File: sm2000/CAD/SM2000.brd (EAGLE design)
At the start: 160 x 160 mm, 405 parts, among them CN1 HDR100-3, CN2 ST-3509, CN3 HDR100-3, CN4 JS-MU3-002, CN5 DS-0518, CN6 ST-3509, CN7 ST-3509, J1 JMP-2PIN, J10 JMPR-2X2, J11 JMPR-2X2, J12 JMPR-2X2, J13 JMPR-2X2, J14 JMPR-2X2, J2 HDR100-7, J3 JMP-2PIN, J4 CONN-BOOM-XH-2A, J5 JMP-2PIN, J6 JMPR-2X2, J7 JMPR-2X2, J8 JMPR-2X2, J9 JMPR-2X2, P6 TPAD50, P7 TPAD50, P8 TPAD50, P9 TPAD50, Q1 MMBT3904, Q10 MMBT3904, Q11 BFR92, Q12 BFQ19, Q13 RD01MUS2, Q14 MMBT3904, Q15 MMBT3904, Q16 MMBT3904, Q17 MMBT3906, Q2 STR2P3LLH6, Q3 MMBT3904, Q4 STR2P3LLH6, Q5 MMBT3904, Q6 MMBT3904, Q7 MMBT3904, Q8 MMBT3904, Q9 MMBT3904, SW1 TS-02B, SW2 SW-LC2259, SW3 TS-026, SW4 TS-026, SW5 SW-LC2259EENP, U1 STM32F405VGT6, U10 LM386M-1, U11 ADE-1, U12 PGA-103+, U13 LMV341, U14 SI5351A, U15 SI570, U16 SA612A, U2 STMPS2141, U3 EMIF02-USB03F2, U4 DNL, U5 L78M09, U6 LD1117AS-33, U7 LMV341, U8 LD1117AS-33, U9 TPS54329E, X1 BU-SMA-H

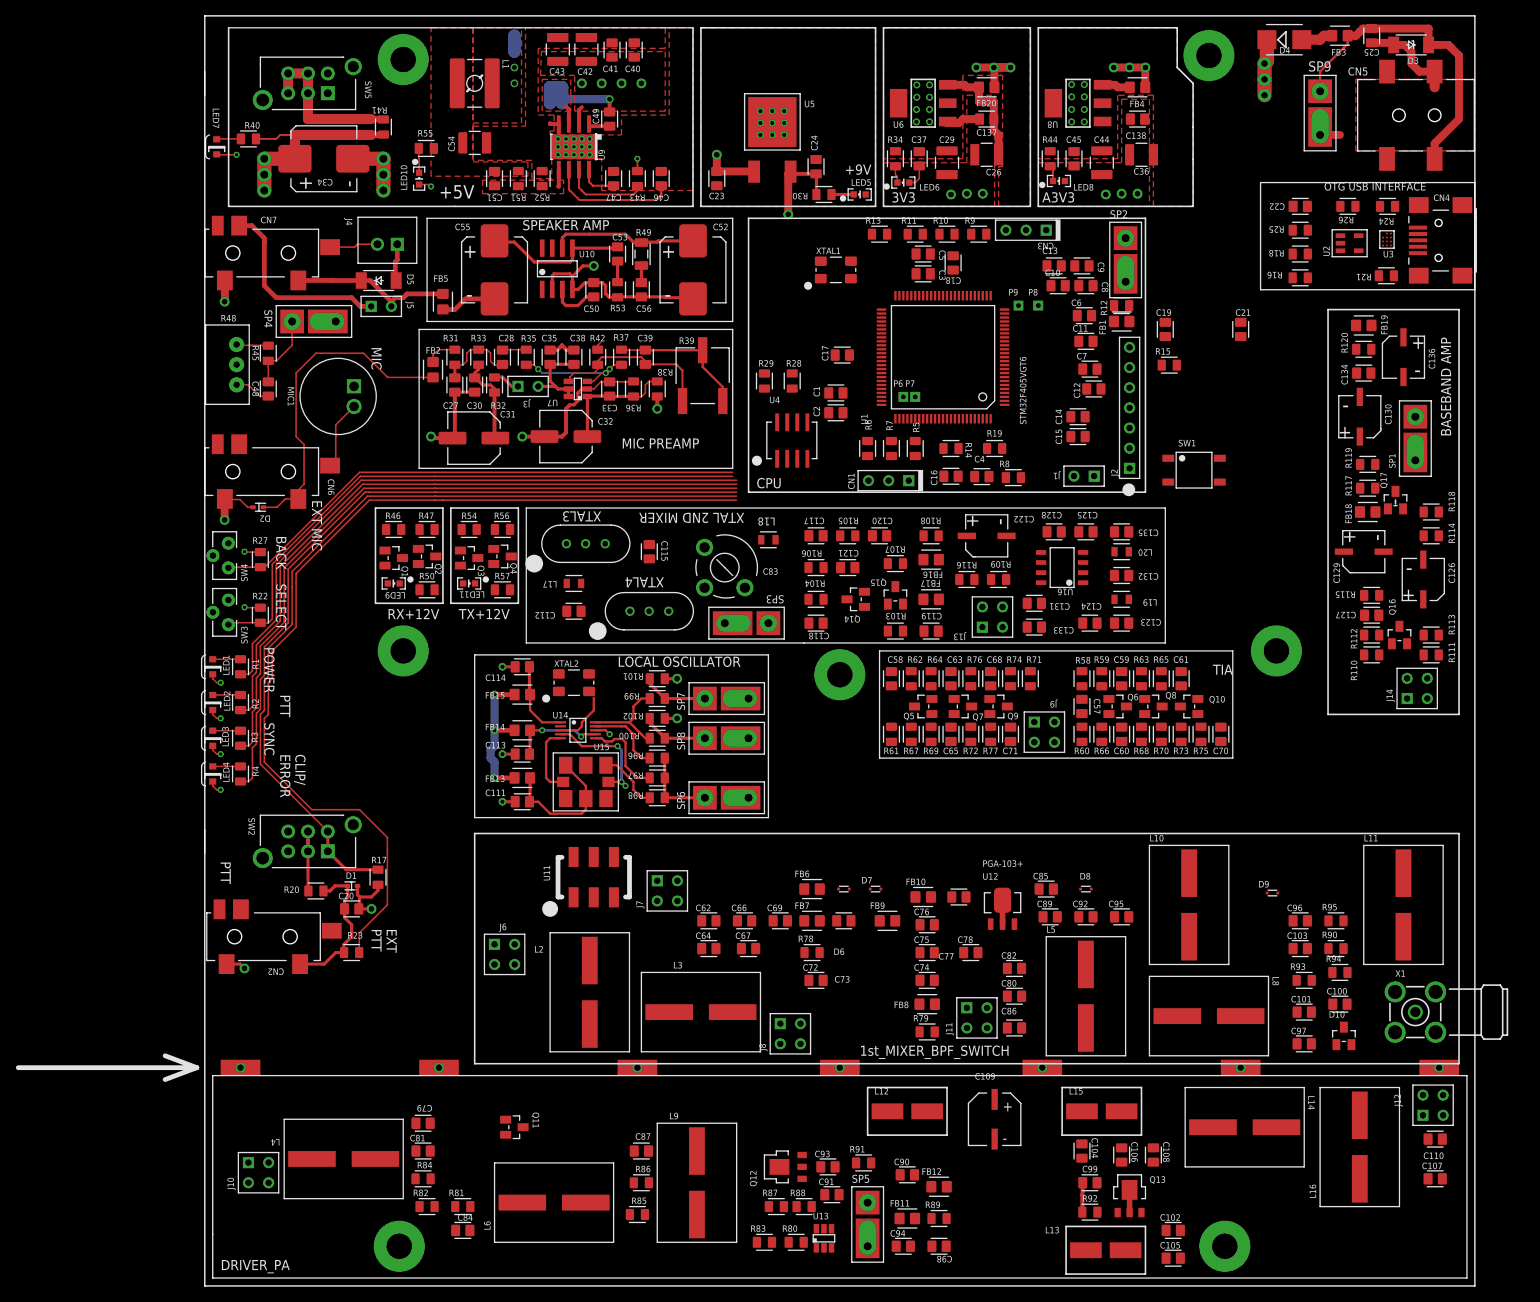
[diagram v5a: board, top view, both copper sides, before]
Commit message: Current status as of 4/4/16 RGB
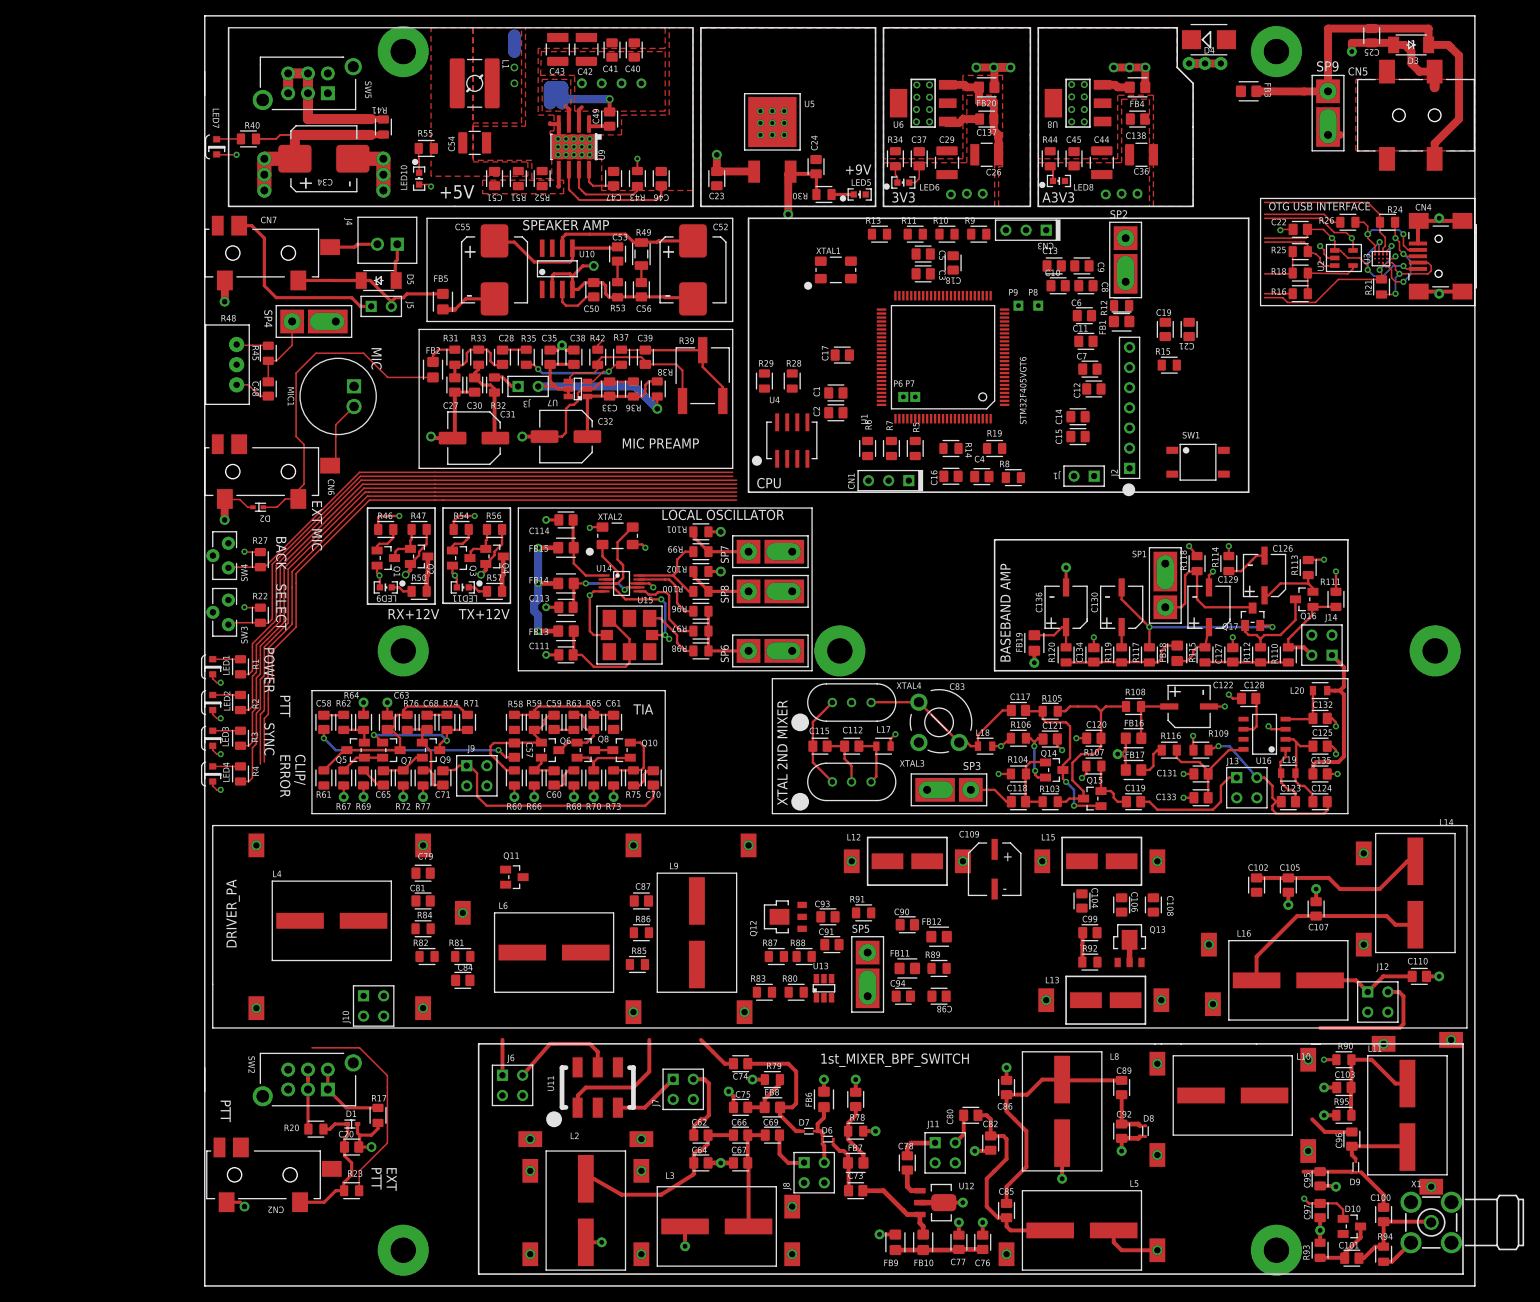
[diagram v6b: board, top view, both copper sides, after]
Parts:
- added PAD1, PAD2, PAD3, PAD4, PAD5, PAD6, PAD7: MTG-PAD-3.2, _RoweTel:MTG-PAD-3.2
- added S10, S11, S12, S13, S14, S15, S16, S17, S18, S19, S20, S21, S22, S23, S24, S25, S26, S27, S28, S29, S30, S31, S32, S33, S34, S35, S36, S8, S9: SGND, _RoweTel:SGND
- moved Q7 72.2 mm to (23.5, 67.5)
- moved C57 71.7 mm to (39.0, 67.5)
- moved C58 71.7 mm to (15.0, 71.0)
- moved C59 71.7 mm to (44.0, 71.0)
- moved C60 71.7 mm to (44.0, 64.0)
- moved C61 71.7 mm to (51.5, 71.0)
- moved C65 71.7 mm to (22.5, 64.0)
- moved C70 71.7 mm to (56.5, 64.0), turned to 90 degrees
- moved C71 71.7 mm to (30.0, 64.0)
- moved J9 71.7 mm to (33.0, 63.0)
- moved Q10 71.7 mm to (52.5, 67.5)
- moved Q5 71.7 mm to (19.0, 67.5)
- moved Q6 71.7 mm to (43.5, 67.5)
- moved Q8 71.7 mm to (48.0, 67.5)
- moved Q9 71.7 mm to (28.5, 67.5)
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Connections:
- net GND: now also PAD1.P$1, PAD2.P$1, PAD3.P$1, PAD4.P$1, PAD5.P$1, PAD6.P$1, PAD7.P$1, S1.1, S10.1, S11.1, S12.1, S13.1, S14.1, S15.1, S16.1, S17.1, S18.1, S19.1, S2.1, S20.1, S21.1, S22.1, S23.1, S24.1, S25.1, S26.1, S27.1, S28.1, S29.1, S3.1, S30.1, S31.1, S32.1, S33.1, S34.1, S35.1, S36.1, S4.1, S5.1, S6.1, S7.1, S8.1, S9.1; no longer S1.SGND, S2.SGND, S3.SGND, S4.SGND, S5.SGND, S6.SGND, S7.SGND
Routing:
- net GND: track 173.1 -> 323.4 mm, vias 50 -> 105
- net TIA_OUT: track 0.00 -> 32.6 mm
- net N$137: track 0.00 -> 31.1 mm
- net TIAIN: track 0.00 -> 30.6 mm, vias 0 -> 2
- net VBUS: track 0.00 -> 30.2 mm, vias 0 -> 4
- net N$92: track 0.00 -> 27.1 mm
- net N$140: track 0.00 -> 26.8 mm
- net N$106: track 0.00 -> 26.1 mm, vias 0 -> 2
- net N$9: track 0.00 -> 25.6 mm
- net N$136: track 0.00 -> 25.5 mm
- net N$21: track 0.00 -> 24.0 mm
- net N$49: track 0.00 -> 22.8 mm, vias 0 -> 1
- net OTG_DM: track 0.00 -> 22.7 mm, vias 0 -> 2
- net N$145: track 0.00 -> 22.7 mm
- net PA_OUTPUT: track 0.00 -> 22.1 mm
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
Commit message: LAYOUT UPDATES as of 4/13/16  RGB 80 NODES to COMPLETE
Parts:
- added S37, S38, S39, S40, S41, S42, S43: SGND, _RoweTel:SGND
- moved R83 87.5 mm to (71.5, 124.5)
- moved U13 85.0 mm to (75.5, 122.5)
- moved R80 84.1 mm to (71.5, 121.0)
- moved J1 41.3 mm to (70.5, 111.0), turned to 0 degrees
- moved C4 36.2 mm to (127.0, 123.6), turned to 90 degrees
- moved R8 35.5 mm to (129.8, 123.6), turned to 270 degrees
- moved XTAL1 35.3 mm to (112.5, 115.5), turned to 270 degrees
- moved C91 28.9 mm to (51.0, 50.0)
- moved R88 27.1 mm to (51.0, 53.0), turned to 180 degrees
- moved SW1 26.5 mm to (128.2, 130.1), turned to 90 degrees
- moved S18 26.2 mm to (77.5, 34.5)
- moved L14 24.5 mm to (128.0, 50.0)
- moved U4 23.0 mm to (72.5, 129.5)
- moved C64 22.3 mm to (41.0, 9.50), turned to 270 degrees
- moved J9 21.8 mm to (53.5, 70.5)
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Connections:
- net GND: now also S37.1, S38.1, S39.1, S40.1, S41.1, S42.1, S43.1
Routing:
- net +9V: track 11.6 -> 296.2 mm, vias 1 -> 5
- net +5V: track 35.6 -> 310.3 mm, vias 9 -> 12
- net TX+12V: track 7.56 -> 256.8 mm, vias 2 -> 11
- net 3V3: track 36.3 -> 216.5 mm, vias 13 -> 22
- net A3V3: track 30.7 -> 168.9 mm, vias 10 -> 15
- net GND: track 323.4 -> 454.2 mm, vias 105 -> 120
- net RX+12V: track 6.01 -> 135.7 mm, vias 1 -> 4
- net +VIN: track 164.7 -> 261.0 mm, vias 11 -> 10
- net RX-2ND-LO: track 10.1 -> 84.7 mm
- net AIN3: track 6.63 -> 78.0 mm, vias 1 -> 2
- net TX-2ND-LO: track 9.99 -> 69.8 mm, vias 1 -> 0
- net 1ST_LO: track 25.8 -> 82.0 mm, vias 0 -> 2
- net !EXT-PTT!: track 111.7 -> 167.4 mm
- net VGG: track 0.00 -> 52.3 mm, vias 0 -> 1
- net DRIVER/PA_INPUT: track 5.34 -> 57.4 mm
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- added copper zone on layer 15, net 3V3
- added copper zone on layer 16, net 3V3
- added copper zone on layer 15, net A3V3
- added copper zone on layer 16, net A3V3
- added copper zone on layer 15, net SW
- removed copper zone on layer 3, net 3V3
- removed copper zone on layer 3, net A3V3
- removed copper zone on layer 3, net SW

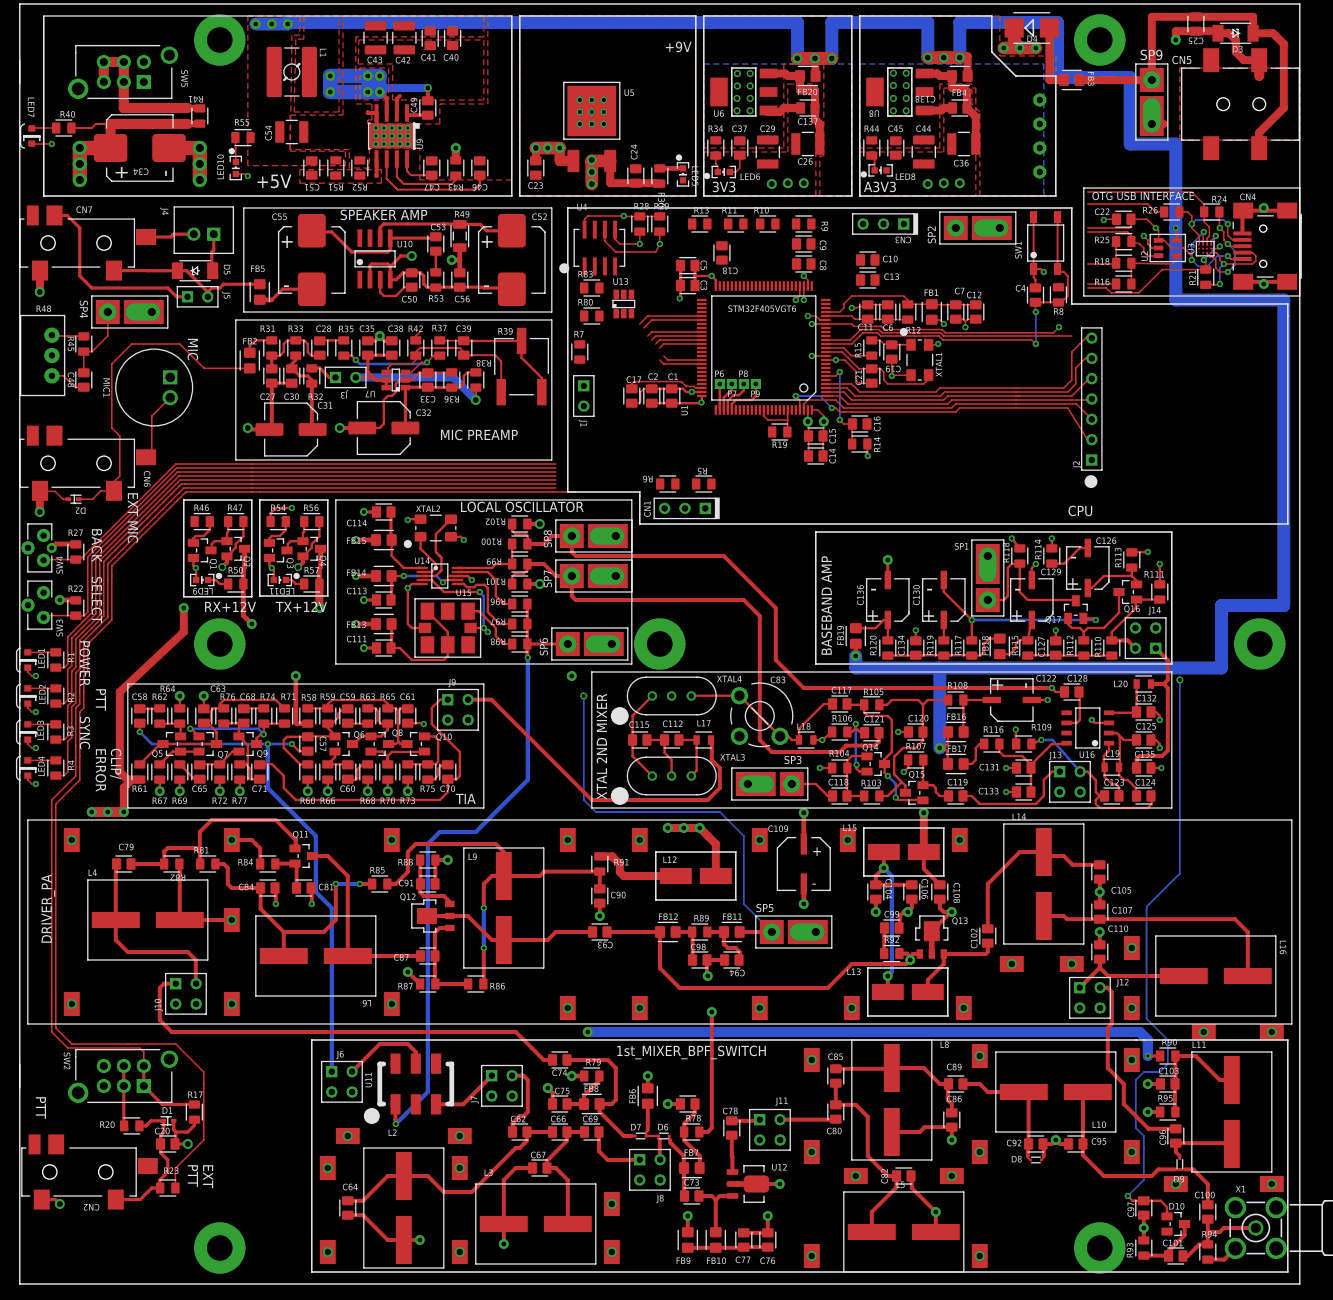
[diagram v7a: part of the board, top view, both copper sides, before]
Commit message: 100% routed, ERC & DRC to follow. BOM, SCH, etc to follow.
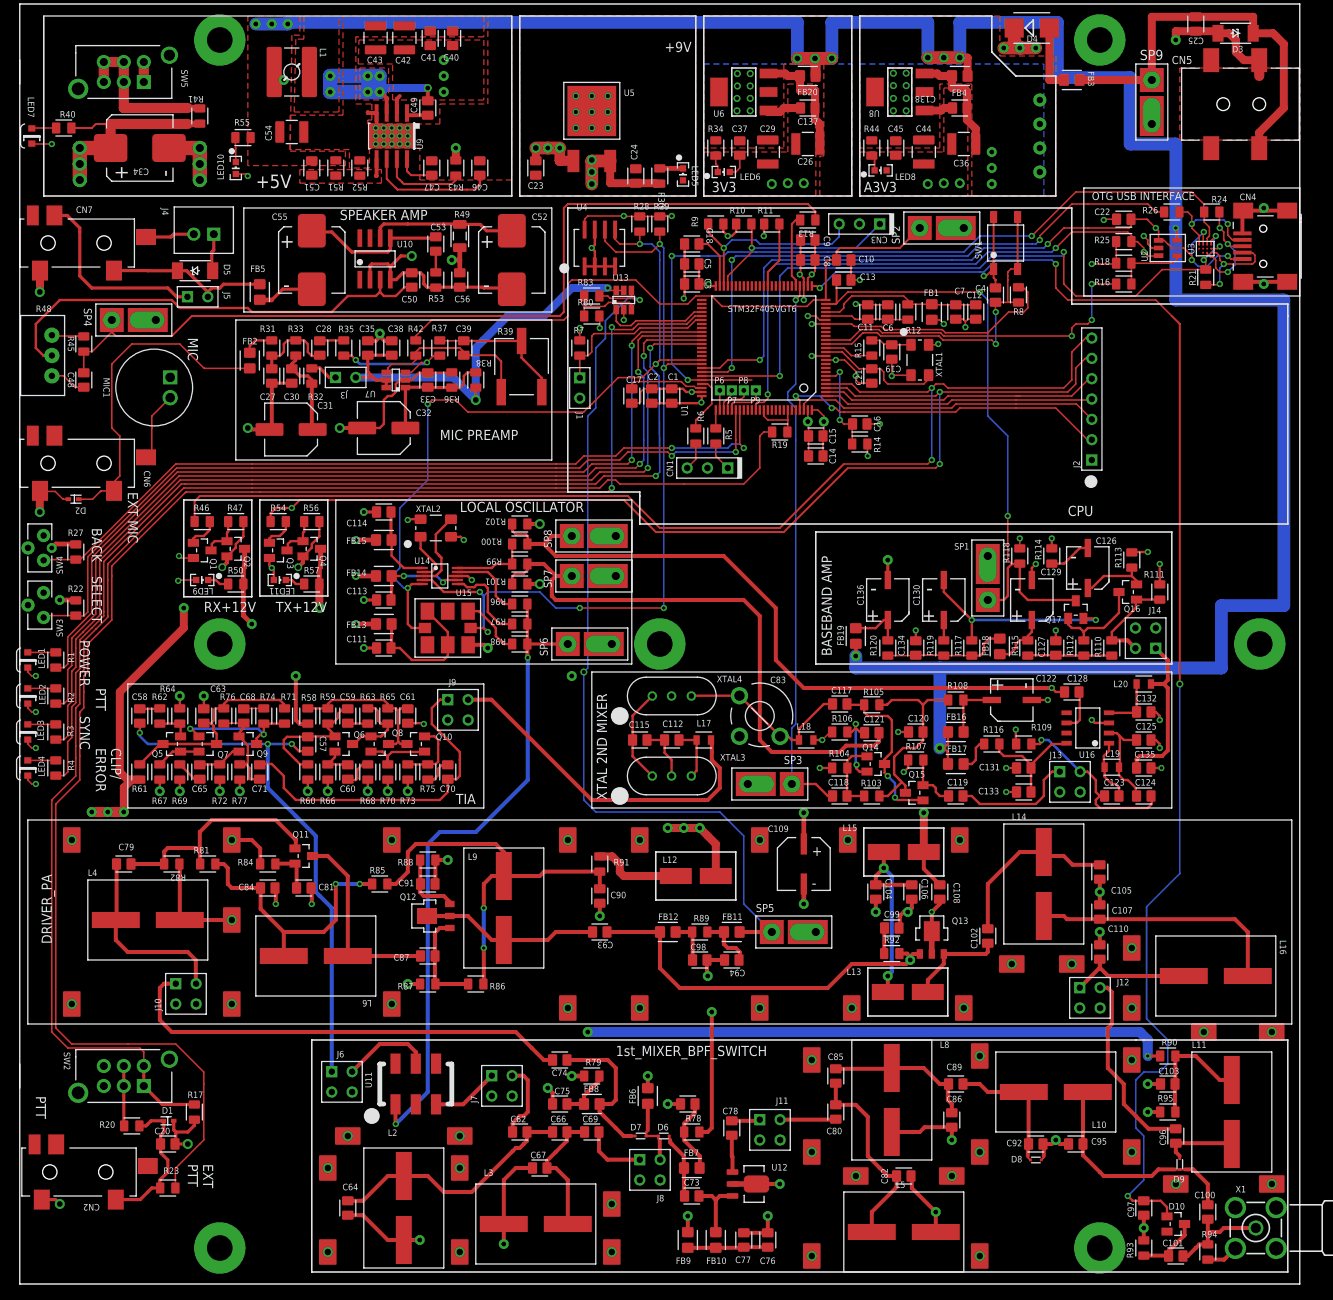
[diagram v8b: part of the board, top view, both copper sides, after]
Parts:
- moved R13 13.5 mm to (98.5, 133.0), turned to 0 degrees
- moved R9 11.0 mm to (87.0, 132.5), turned to 180 degrees
- moved R6 6.95 mm to (84.5, 106.0), turned to 270 degrees
- moved R5 6.18 mm to (87.0, 106.0), turned to 270 degrees
- moved CN1 5.78 mm to (88.5, 102.0)
- moved R8 5.00 mm to (124.8, 123.6)
- moved C4 5.00 mm to (122.0, 123.6)
- moved SW1 5.00 mm to (123.2, 130.1)
- moved R11 4.50 mm to (94.0, 132.5)
- moved SP2 4.50 mm to (114.0, 132.0)
- moved C18 3.93 mm to (84.0, 130.0), turned to 180 degrees
- moved C10 3.00 mm to (103.0, 128.0)
- moved C13 3.00 mm to (103.0, 125.5)
- moved CN3 3.00 mm to (107.5, 132.5)
- moved R10 3.00 mm to (90.5, 132.5)
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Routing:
- net +12VRXENB: track 38.5 -> 148.1 mm, vias 0 -> 2
- net DAC2_OUT: track 9.46 -> 114.2 mm
- net A3V3: track 168.9 -> 266.8 mm, vias 15 -> 19
- net AIN3: track 78.0 -> 175.1 mm, vias 2 -> 4
- net +12VTXENB: track 40.8 -> 136.3 mm, vias 1 -> 3
- net OTG_DP: track 20.6 -> 100.3 mm, vias 0 -> 3
- net AIN2: track 1.26 -> 78.5 mm
- net SDA3: track 19.9 -> 95.4 mm, vias 2 -> 4
- net SCL3: track 32.1 -> 100.6 mm, vias 4 -> 6
- net OTG_DM: track 22.7 -> 89.5 mm, vias 2 -> 4
- net OTG_ID: track 9.96 -> 75.1 mm, vias 0 -> 3
- net VBUS: track 30.2 -> 92.1 mm, vias 4 -> 6
- net TX_DAC: track 7.68 -> 69.2 mm
- net OTG_OVR_CUR: track 11.5 -> 71.3 mm, vias 0 -> 3
- net VGG: track 52.3 -> 112.1 mm, vias 1 -> 2
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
